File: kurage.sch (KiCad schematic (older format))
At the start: 106 parts, among them SW1 ESC, SW10 R, SW11 Y, SW12 I, SW13 P, SW14 ], SW15 UNDEFINED2, SW16 CTRL, SW17 A, SW18 D, SW19 G, SW2 Q, SW20 J, SW21 L, SW22 ', SW23 S, SW24 F, SW25 H, SW26 K, SW27 ;, SW28 ENTER, SW29 UNDEFINED3, SW3 E, SW30 LSHIFT, SW31 Z, SW32 C, SW33 B, SW34 M, SW35 ., SW36 LSHIFT, SW37 X, SW38 V, SW39 N, SW4 T, SW40 ,, SW41 /, SW42 UP, SW43 LOWER, SW44 UNDEFINED1, SW45 WIN, SW46 RAISE, SW47 LEFT, SW48 RIGHT, SW49 LSPACE, SW5 U, SW50 RSPACE, SW51 ALT, SW52 DOWN, SW6 O, SW7 [, SW8 BACKSPACE, SW9 W, U1 Elite-C

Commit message: schematic
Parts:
- D1, D10, D11, D12, D13, D14, D15, D16, D17, D18, D19, D2, D20, D21, D22, D23, D24, D25, D26, D27, D28, D29, D3, D30, D31, D32, D33, D34, D35, D36, D37, D38, D39, D4, D40, D41, D42, D43, D44, D45, D46, D47, D48, D49, D5, D50, D51, D6, D7, D8, D9: footprint (none) -> kbd:D3_TH
- D52, OL1, SW1, SW10, SW11, SW12, SW13, SW14, SW15, SW16, SW17, SW18, SW19, SW2, SW20, SW21, SW22, SW23, SW24, SW25, SW26, SW27, SW28, SW29, SW3, SW30, SW31, SW32, SW33, SW34, SW35, SW36, SW37, SW38, SW39, SW4, SW40, SW41, SW42, SW43, SW44, SW45, SW46, SW47, SW48, SW49, SW5, SW50, SW51, SW52, SW6, SW7, SW8, SW9: footprint (none) -> kbd:CherryMX_Hotswap
- U1: footprint (none) -> Keebio-Parts:Elite-C

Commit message: pcb
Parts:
- D52: footprint kbd:CherryMX_Hotswap -> kbd:D3_TH
- OL1: footprint kbd:CherryMX_Hotswap -> kbd:OLED_v2
- SW1, SW10, SW11, SW12, SW13, SW14, SW15, SW16, SW17, SW18, SW19, SW2, SW20, SW21, SW22, SW23, SW24, SW25, SW26, SW27, SW28, SW29, SW3, SW30, SW31, SW32, SW33, SW34, SW35, SW37, SW38, SW39, SW4, SW40, SW41, SW42, SW43, SW44, SW45, SW46, SW47, SW48, SW49, SW5, SW50, SW51, SW52, SW6, SW7, SW8, SW9: footprint kbd:CherryMX_Hotswap -> MX_Only:MXOnly-1U-Hotswap
- SW36: value LSHIFT -> RSHIFT; footprint kbd:CherryMX_Hotswap -> MX_Only:MXOnly-1U-Hotswap

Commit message: progress
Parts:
- SW1, SW44, SW46: footprint MX_Only:MXOnly-1U-Hotswap -> MX_Only:MXOnly-1.5U-Hotswap
- SW16, SW8: footprint MX_Only:MXOnly-1U-Hotswap -> MX_Only:MXOnly-1.75U-Hotswap
- SW28, SW30: footprint MX_Only:MXOnly-1U-Hotswap -> MX_Only:MXOnly-2.25U-Hotswap
- SW36, SW49: footprint MX_Only:MXOnly-1U-Hotswap -> MX_Only:MXOnly-2U-Hotswap
- SW43: footprint MX_Only:MXOnly-1U-Hotswap -> MX_Only:MXOnly-1.25U-Hotswap
- SW50: footprint MX_Only:MXOnly-1U-Hotswap -> MX_Only:MXOnly-2.75U-Hotswap
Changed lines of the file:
@@
 F 0 "SW44" H 4600 4055 50  0000 C CNN
 F 1 "UNDEFINED1" H 4600 3964 50  0000 C CNN
-F 2 "MX_Only:MXOnly-1U-Hotswap" H 4600 3800 50  0001 C CNN
+F 2 "MX_Only:MXOnly-1.5U-Hotswap" H 4600 3800 50  0001 C CNN
 F 3 "" H 4600 3800 50  0000 C CNN
 	1    4600 3800
@@
 F 0 "SW49" H 4600 4455 50  0000 C CNN
 F 1 "LSPACE" H 4600 4364 50  0000 C CNN
-F 2 "MX_Only:MXOnly-1U-Hotswap" H 4600 4200 50  0001 C CNN
+F 2 "MX_Only:MXOnly-2U-Hotswap" H 4600 4200 50  0001 C CNN
 F 3 "" H 4600 4200 50  0000 C CNN
 	1    4600 4200
@@
 F 0 "SW46" H 6600 4055 50  0000 C CNN
 F 1 "RAISE" H 6600 3964 50  0000 C CNN
-F 2 "MX_Only:MXOnly-1U-Hotswap" H 6600 3800 50  0001 C CNN
+F 2 "MX_Only:MXOnly-1.5U-Hotswap" H 6600 3800 50  0001 C CNN
 F 3 "" H 6600 3800 50  0000 C CNN
 	1    6600 3800
@@
 F 0 "SW28" H 8600 2855 50  0000 C CNN
 F 1 "ENTER" H 8600 2764 50  0000 C CNN
-F 2 "MX_Only:MXOnly-1U-Hotswap" H 8600 2600 50  0001 C CNN
+F 2 "MX_Only:MXOnly-2.25U-Hotswap" H 8600 2600 50  0001 C CNN
 F 3 "" H 8600 2600 50  0000 C CNN
 	1    8600 2600
@@
 F 0 "SW36" H 8600 3255 50  0000 C CNN
 F 1 "RSHIFT" H 8600 3164 50  0000 C CNN
-F 2 "MX_Only:MXOnly-1U-Hotswap" H 8600 3000 50  0001 C CNN
+F 2 "MX_Only:MXOnly-2U-Hotswap" H 8600 3000 50  0001 C CNN
 F 3 "" H 8600 3000 50  0000 C CNN
 	1    8600 3000
@@
 F 0 "SW8" H 9600 1655 50  0000 C CNN
 F 1 "BACKSPACE" H 9600 1564 50  0000 C CNN
-F 2 "MX_Only:MXOnly-1U-Hotswap" H 9600 1400 50  0001 C CNN
+F 2 "MX_Only:MXOnly-1.75U-Hotswap" H 9600 1400 50  0001 C CNN
 F 3 "" H 9600 1400 50  0000 C CNN
 	1    9600 1400
@@
 F 0 "SW43" H 2600 4055 50  0000 C CNN
 F 1 "LOWER" H 2600 3964 50  0000 C CNN
-F 2 "MX_Only:MXOnly-1U-Hotswap" H 2600 3800 50  0001 C CNN
+F 2 "MX_Only:MXOnly-1.25U-Hotswap" H 2600 3800 50  0001 C CNN
 F 3 "" H 2600 3800 50  0000 C CNN
 	1    2600 3800
@@
 F 0 "SW30" H 2600 3255 50  0000 C CNN
 F 1 "LSHIFT" H 2600 3164 50  0000 C CNN
-F 2 "MX_Only:MXOnly-1U-Hotswap" H 2600 3000 50  0001 C CNN
+F 2 "MX_Only:MXOnly-2.25U-Hotswap" H 2600 3000 50  0001 C CNN
 F 3 "" H 2600 3000 50  0000 C CNN
 	1    2600 3000
@@
 F 0 "SW16" H 2600 2455 50  0000 C CNN
 F 1 "CTRL" H 2600 2364 50  0000 C CNN
-F 2 "MX_Only:MXOnly-1U-Hotswap" H 2600 2200 50  0001 C CNN
+F 2 "MX_Only:MXOnly-1.75U-Hotswap" H 2600 2200 50  0001 C CNN
 F 3 "" H 2600 2200 50  0000 C CNN
 	1    2600 2200
@@
 F 0 "SW1" H 2600 1655 50  0000 C CNN
 F 1 "ESC" H 2600 1564 50  0000 C CNN
-F 2 "MX_Only:MXOnly-1U-Hotswap" H 2600 1400 50  0001 C CNN
+F 2 "MX_Only:MXOnly-1.5U-Hotswap" H 2600 1400 50  0001 C CNN
 F 3 "" H 2600 1400 50  0000 C CNN
 	1    2600 1400
@@
 F 0 "SW50" H 5600 4455 50  0000 C CNN
 F 1 "RSPACE" H 5600 4364 50  0000 C CNN
-F 2 "MX_Only:MXOnly-1U-Hotswap" H 5600 4200 50  0001 C CNN
+F 2 "MX_Only:MXOnly-2.75U-Hotswap" H 5600 4200 50  0001 C CNN
 F 3 "" H 5600 4200 50  0000 C CNN
 	1    5600 4200

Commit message: save
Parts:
- removed U1: Elite-C, Keebio-Parts:Elite-C, symbol keebio:Elite-C
- added U1: ProMicro, kbd:ProMicro_v3, symbol kbd:ProMicro
- SW10, SW11, SW12, SW13, SW14, SW15, SW17, SW18, SW19, SW2, SW20, SW21, SW22, SW23, SW24, SW25, SW26, SW27, SW29, SW3, SW31, SW32, SW33, SW34, SW35, SW37, SW38, SW39, SW4, SW40, SW41, SW42, SW45, SW47, SW48, SW5, SW51, SW52, SW6, SW7, SW9: footprint MX_Only:MXOnly-1U-Hotswap -> kbd:CherryMX_Hotswap
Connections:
- net +5V: now also U1.21 (VCC)
- net COL0: now also U1.20 (F4/A3)
- net COL1: now also U1.19 (F5/A2)
- net COL2: now also U1.18 (F6/A1)
- net COL3: now also U1.17 (F7/A0)
- net COL4: now also U1.16 (B1/15)
- net COL5: now also U1.15 (B3/14)
- net COL6: now also U1.14 (B2/16)
- net COL7: now also U1.13 (B6/10)
- net GND: now also U1.23 (GND), U1.3 (GND), U1.4 (GND)
- net ROW0: now also U1.1 (TX0/D3)
- net ROW1: now also U1.2 (RX1/D2)
- net ROW2: now also U1.8 (5/C6)
- net ROW3: now also U1.7 (4/D4)
- net ROW4: now also U1.10 (7/E6)
- net ROW5: now also U1.9 (6/D7)
- net ROW6: now also U1.12 (9/B5)
- net ROW7: now also U1.11 (8/B4)
- net SCL: now also U1.6 (3/D0/SCL)
- net SDA: now also U1.5 (2/D1/SDA)

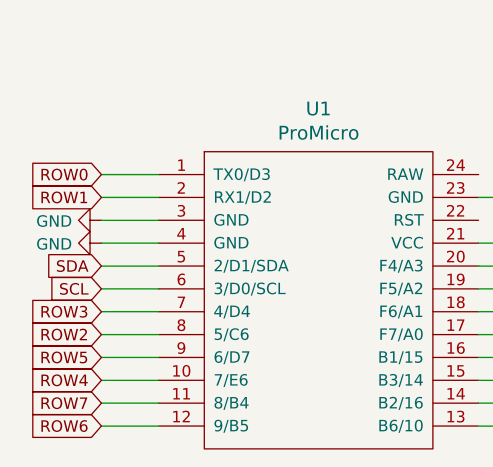
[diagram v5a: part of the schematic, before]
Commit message: flip pro micro
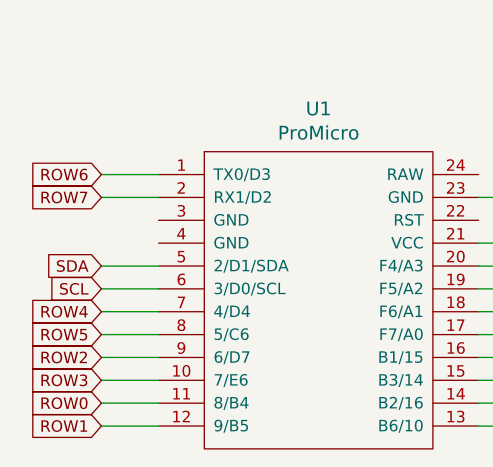
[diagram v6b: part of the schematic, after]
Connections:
- net GND: no longer U1.3 (GND), U1.4 (GND)
- net ROW0: now also U1.11 (8/B4); no longer U1.1 (TX0/D3)
- net ROW1: now also U1.12 (9/B5); no longer U1.2 (RX1/D2)
- net ROW2: now also U1.9 (6/D7); no longer U1.8 (5/C6)
- net ROW3: now also U1.10 (7/E6); no longer U1.7 (4/D4)
- net ROW4: now also U1.7 (4/D4); no longer U1.10 (7/E6)
- net ROW5: now also U1.8 (5/C6); no longer U1.9 (6/D7)
- net ROW6: now also U1.1 (TX0/D3); no longer U1.12 (9/B5)
- net ROW7: now also U1.2 (RX1/D2); no longer U1.11 (8/B4)
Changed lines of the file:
@@
 SCL
-Wire Wire Line
-	1400 6000 1650 6000
-Wire Wire Line
-	1400 5900 1650 5900
-$Comp
-L power:GND #PWR04
-U 1 1 5F757B79
-P 1400 6000
-F 0 "#PWR04" H 1400 5750 50  0001 C CNN
-F 1 "GND" V 1405 5872 50  0000 R CNN
-F 2 "" H 1400 6000 50  0001 C CNN
-F 3 "" H 1400 6000 50  0001 C CNN
-	1    1400 6000
-	0    1    1    0
-$EndComp
-$Comp
-L power:GND #PWR02
-U 1 1 5F756E27
-P 1400 5900
-F 0 "#PWR02" H 1400 5650 50  0001 C CNN
-F 1 "GND" V 1405 5772 50  0000 R CNN
-F 2 "" H 1400 5900 50  0001 C CNN
-F 3 "" H 1400 5900 50  0001 C CNN
-	1    1400 5900
-	0    1    1    0
-$EndComp
 Wire Wire Line
 	3300 6000 3050 6000
@@
 Wire Wire Line
 	3050 6100 3300 6100
-Text GLabel 1400 6800 0    50   Input ~ 0
-ROW6
-Text GLabel 1400 6700 0    50   Input ~ 0
-ROW7
-Text GLabel 1400 6500 0    50   Input ~ 0
-ROW5
-Text GLabel 1400 6600 0    50   Input ~ 0
-ROW4
-Text GLabel 1400 6300 0    50   Input ~ 0
-ROW3
-Text GLabel 1400 6400 0    50   Input ~ 0
-ROW2
-Text GLabel 1400 5800 0    50   Input ~ 0
-ROW1
-Text GLabel 1400 5700 0    50   Input ~ 0
-ROW0
 Wire Wire Line
 	1400 6800 1650 6800
@@
 Wire Wire Line
 	1650 5700 1400 5700
+Text GLabel 1400 6600 0    50   Input ~ 0
+ROW3
+Text GLabel 1400 6500 0    50   Input ~ 0
+ROW2
+Text GLabel 1400 6800 0    50   Input ~ 0
+ROW1
+Text GLabel 1400 6400 0    50   Input ~ 0
+ROW5
+Text GLabel 1400 6300 0    50   Input ~ 0
+ROW4
+Text GLabel 1400 5800 0    50   Input ~ 0
+ROW7
+Text GLabel 1400 5700 0    50   Input ~ 0
+ROW6
+Text GLabel 1400 6700 0    50   Input ~ 0
+ROW0
 $EndSCHEMATC

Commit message: progress
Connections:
- net ROW6: now also U1.2 (RX1/D2); no longer U1.1 (TX0/D3)
- net ROW7: now also U1.1 (TX0/D3); no longer U1.2 (RX1/D2)
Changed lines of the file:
@@
 Text GLabel 1400 6300 0    50   Input ~ 0
 ROW4
+Text GLabel 1400 5700 0    50   Input ~ 0
+ROW7
 Text GLabel 1400 5800 0    50   Input ~ 0
-ROW7
-Text GLabel 1400 5700 0    50   Input ~ 0
 ROW6
 Text GLabel 1400 6700 0    50   Input ~ 0
